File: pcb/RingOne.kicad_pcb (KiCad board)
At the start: 4 copper layers, 0 parts

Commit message: PCB: routing of all components
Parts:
- added BT1: 1S Li-Po, TCY_connectors:Amphenol_10114830-11102LF_1x02_P1.25mm_Horizontal, F.Cu at (126.7, 90.5)
- added C1: 10uF, Capacitor_SMD:C_0805_2012Metric, F.Cu at (127.0, 101.0)
- added C10: 100nF, TCY_passives:C_0603_1608Metric, F.Cu at (129.0, 95.9)
- added C11: 100nF, Capacitor_SMD:C_0603_1608Metric, B.Cu at (131.5, 99.8)
- added C12: 100nF, Capacitor_SMD:C_0603_1608Metric, F.Cu at (114.4, 102.0)
- added C13: 1uF, Capacitor_SMD:C_0603_1608Metric, F.Cu at (110.8, 88.1)
- added C14: 1uF, Capacitor_SMD:C_0603_1608Metric, F.Cu at (121.7, 87.6)
- added C15: 1uF, Capacitor_SMD:C_0603_1608Metric, F.Cu at (116.3, 86.8)
- added C16: 1uF, Capacitor_SMD:C_0603_1608Metric, F.Cu at (119.4, 86.8)
- added C17: 1uF, Capacitor_SMD:C_0603_1608Metric, B.Cu at (110.5, 88.3)
- added C18: 4.7uF, Capacitor_SMD:C_0603_1608Metric, B.Cu at (132.2, 87.6)
- added C19: 4.7uF, Capacitor_SMD:C_0603_1608Metric, B.Cu at (133.8, 87.6)
- added C2: 100nF, Capacitor_SMD:C_0603_1608Metric, F.Cu at (126.7, 97.3)
- added C20: 100nF, Capacitor_SMD:C_0603_1608Metric, B.Cu at (126.6, 93.0)
- added C21: 100nF, Capacitor_SMD:C_0603_1608Metric, B.Cu at (128.4, 102.8)
- added C22: 1uF, Capacitor_SMD:C_0603_1608Metric, B.Cu at (117.9, 95.5)
- added C23: 100nF, Capacitor_SMD:C_0603_1608Metric, F.Cu at (130.2, 102.0)
- added C24: 100nF, Capacitor_SMD:C_0603_1608Metric, B.Cu at (122.2, 96.3)
- added C25: 1uF, Capacitor_SMD:C_0603_1608Metric, B.Cu at (117.9, 101.3)
- added C26: 1uF, Capacitor_SMD:C_0603_1608Metric, B.Cu at (120.4, 101.8)
- added C27: 1uF, Capacitor_SMD:C_0603_1608Metric, B.Cu at (123.2, 101.8)
- added C3: 100nF, Capacitor_SMD:C_0603_1608Metric, F.Cu at (115.2, 95.7)
- added C4: 100nF, Capacitor_SMD:C_0603_1608Metric, F.Cu at (126.7, 102.8)
- added C5: 100nF, Capacitor_SMD:C_0603_1608Metric, F.Cu at (115.2, 98.8)
- added C6: 100nF, Capacitor_SMD:C_0603_1608Metric, F.Cu at (132.5, 101.2)
- added C7: 100nF, Capacitor_SMD:C_0603_1608Metric, B.Cu at (106.9, 103.2)
- added C8: 100nF, Capacitor_SMD:C_0603_1608Metric, F.Cu at (132.2, 87.9)
- added C9: 100nF, TCY_passives:C_0603_1608Metric, F.Cu at (129.0, 93.5)
- added D1: LED_RGBA, Resistor_SMD:R_Array_Convex_2x0606, F.Cu at (135.9, 87.9)
- added D2: EADA25L, Package_TO_SOT_SMD:SOT-23, B.Cu at (109.0, 93.5)
- added D3: RB751S40T5G, Diode_SMD:D_SOD-523, B.Cu at (129.5, 99.0)
- added D4: RB751S40T5G, Diode_SMD:D_SOD-523, B.Cu at (129.5, 100.6)
- added D5: 3V3, Diode_SMD:D_SOD-523, B.Cu at (129.5, 97.4)
- added D6: 3V3, Diode_SMD:D_SOD-523, B.Cu at (123.7, 96.3)
- added FB1: 50R@100Mhz, Inductor_SMD:L_1206_3216Metric, B.Cu at (109.0, 101.2)
- added J1: PROG_CONN, TCY_connectors:Amphenol_10114830-11103LF_1x03_P1.25mm_Horizontal, B.Cu at (126.5, 90.6)
- added J2: DBG_UART, TCY_connectors:Amphenol_10114830-11103LF_1x03_P1.25mm_Horizontal, B.Cu at (116.5, 90.6)
- added J3: USB_C_Receptacle_USB2.0, Connector_USB:USB_C_Receptacle_HRO_TYPE-C-31-M-12, F.Cu at (109.0, 95.0)
- added Q1: YJQ3400, TCY_IC:UDFN-6-2EP_2x2mm_P0.65mm_EP1x0.7mm, B.Cu at (129.7, 94.0)
- added Q2: UT6MA2TCR, TCY_IC:UDFN-6-2EP_2x2mm_P0.65mm_EP1x0.7mm, B.Cu at (126.6, 96.7)
- added R1: 100k, Resistor_SMD:R_0603_1608Metric, B.Cu at (105.9, 100.9)
- added R10: 330R, Resistor_SMD:R_0603_1608Metric, F.Cu at (129.5, 91.4)
- added R11: 2k2, Resistor_SMD:R_0603_1608Metric, B.Cu at (126.6, 94.7)
- added R12: 470k, Resistor_SMD:R_0603_1608Metric, B.Cu at (126.7, 100.7)
- added R13: 470k, Resistor_SMD:R_0603_1608Metric, B.Cu at (126.7, 99.2)
- added R14: 10k, Resistor_SMD:R_0603_1608Metric, F.Cu at (130.6, 97.4)
- added R15: 10k, Resistor_SMD:R_0603_1608Metric, F.Cu at (130.6, 94.5)
- added R16: 100k, Resistor_SMD:R_0603_1608Metric, B.Cu at (117.0, 93.6)
- added R17: 1k, Resistor_SMD:R_0603_1608Metric, F.Cu at (132.5, 102.8)
- added R18: 0.05R, Resistor_SMD:R_0603_1608Metric, B.Cu at (120.7, 98.8)
- added R19: 10k, Resistor_SMD:R_0603_1608Metric, B.Cu at (132.3, 97.4)
- added R2: 1k, Resistor_SMD:R_0603_1608Metric, B.Cu at (109.9, 103.2)
- added R3: 22R, Resistor_SMD:R_0603_1608Metric, B.Cu at (106.0, 94.4)
- added R4: 22R, Resistor_SMD:R_0603_1608Metric, B.Cu at (106.0, 97.4)
- added R5: 1k, Resistor_SMD:R_0603_1608Metric, B.Cu at (108.9, 88.3)
- added R6: 10k, TCY_passives:R_0603_1608Metric, F.Cu at (108.3, 88.7)
- added R7: 1k, TCY_passives:R_0603_1608Metric, F.Cu at (108.3, 87.6)
- added R8: 22k, Resistor_SMD:R_0603_1608Metric, B.Cu at (135.1, 91.5)
- added R9: 100k, Resistor_SMD:R_0603_1608Metric, B.Cu at (133.0, 89.9)
- added SW1: RST_BTN, TCY_buttons_switches:KMT031NGJLHS, F.Cu at (107.2, 102.0)
- added SW2: WAKEUP, TCY_buttons_switches:EVQ-P7J01P, F.Cu at (136.8, 102.4)
- added TP1: VBUS, TCY_connectors:TestPoint_Pad_D0.5mm, F.Cu at (106.5, 89.1)
- added TP2: TestPoint, TCY_connectors:TestPoint_Pad_D0.5mm, B.Cu at (126.3, 101.9)
- added TP3: TestPoint, TCY_connectors:TestPoint_Pad_D0.5mm, B.Cu at (132.8, 96.1)
- added U1: STM32L452CEUx, Package_DFN_QFN:QFN-48-1EP_7x7mm_P0.5mm_EP5.6x5.6mm, F.Cu at (120.4, 99.1)
- added U10: MCP73831-2-OT, Package_TO_SOT_SMD:SOT-23-5, B.Cu at (136.2, 88.2)
- added U11: BQ297xy, Package_SON:WSON-6_1.5x1.5mm_P0.5mm, B.Cu at (129.8, 91.6)
- added U12: LM66100, Package_TO_SOT_SMD:SOT-363_SC-70-6, B.Cu at (113.9, 93.5)
- added U13: LM66100, Package_TO_SOT_SMD:SOT-363_SC-70-6, B.Cu at (113.9, 96.5)
- added U14: SN74LVC1G14DRL, Package_TO_SOT_SMD:SOT-553, B.Cu at (131.1, 102.5)
- added U15: NCV8165ML330, Package_DFN_QFN:DFN-8-1EP_3x3mm_P0.65mm_EP1.55x2.4mm, B.Cu at (118.2, 98.5)
- added U16: INA199, Package_DFN_QFN:UQFN-10_1.4x1.8mm_P0.4mm, B.Cu at (122.8, 99.0)
- added U17: MIC94300, TCY_IC:MLF-4_1.2x1.6mm_P0.5_1EP_0.85x0.5mm, B.Cu at (121.8, 101.7)
- added U2: RN4871, RF_Module:Microchip_RN4871, F.Cu at (136.0, 95.0)
- added U3: M24C32-FMC6TG, Package_DFN_QFN:DFN-8-1EP_3x2mm_P0.5mm_EP1.3x1.5mm, F.Cu at (111.5, 102.0)
- added U4: KTD2026BEWE, TCY_IC:UTDFN-8-1EP_1.5x1.5mm_P0.4mm_EP0.8x1.45mm, F.Cu at (133.9, 88.2)
- added U5: LSM6DSL, Package_LGA:LGA-14_3x2.5mm_P0.5mm_LayoutBorder3x4y, F.Cu at (126.7, 94.5)
- added U6: AT25SF321B, Package_DFN_QFN:DFN-8-1EP_6x5mm_P1.27mm_EP4x4mm, B.Cu at (136.0, 101.0)
- added U7: USBLC6-2SC6, Package_TO_SOT_SMD:SOT-23-6, B.Cu at (109.0, 97.0)
- added U8: PMDPB70XP, TCY_IC:UDFN-6-2EP_2x2mm_P0.65mm_EP1x0.7mm, F.Cu at (113.0, 88.0)
- added U9: STUSB1600AQTR, Package_DFN_QFN:QFN-24-1EP_4x4mm_P0.5mm_EP2.7x2.7mm, F.Cu at (118.3, 90.2)
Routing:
- net GND: track 0.00 -> 171.3 mm, vias 0 -> 70
- net +3V3: track 0.00 -> 118.5 mm, vias 0 -> 10
- net +BATT: track 0.00 -> 53.3 mm, vias 0 -> 5
- net /PER_PWR: track 0.00 -> 52.5 mm, vias 0 -> 4
- net /SDA: track 0.00 -> 44.4 mm, vias 0 -> 3
- net /SCL: track 0.00 -> 43.2 mm, vias 0 -> 3
- net VBUS: track 0.00 -> 40.1 mm, vias 0 -> 3
- net /RESET: track 0.00 -> 36.7 mm, vias 0 -> 3
- net VCC: track 0.00 -> 34.8 mm, vias 0 -> 2
- net /CHARG_STAT: track 0.00 -> 33.6 mm, vias 0 -> 2
- net +5V: track 0.00 -> 33.1 mm, vias 0 -> 5
- net /MOSI: track 0.00 -> 32.5 mm, vias 0 -> 2
- net /SCK: track 0.00 -> 29.6 mm, vias 0 -> 4
- net /Power_management/PWR_EN: track 0.00 -> 29.4 mm, vias 0 -> 2
- net /MISO: track 0.00 -> 23.2 mm, vias 0 -> 2
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- added copper zone on B.Cu, net GND
- added copper zone on F.Cu, net GND
- added copper zone on In1.Cu, net GND
- added copper zone on In2.Cu, net GND
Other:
- board outline added: 35 x 18 mm
- board text added: "JLCJLCJLCJLC"

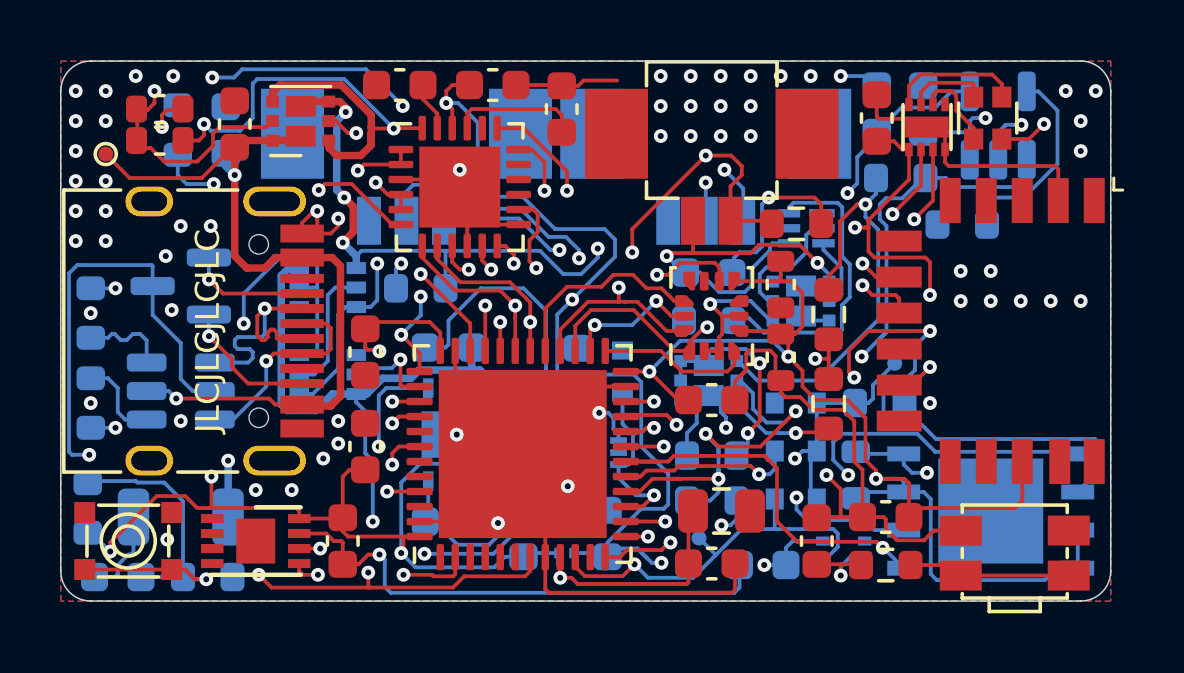
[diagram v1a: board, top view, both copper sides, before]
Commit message: PCB & Schema: update page layout
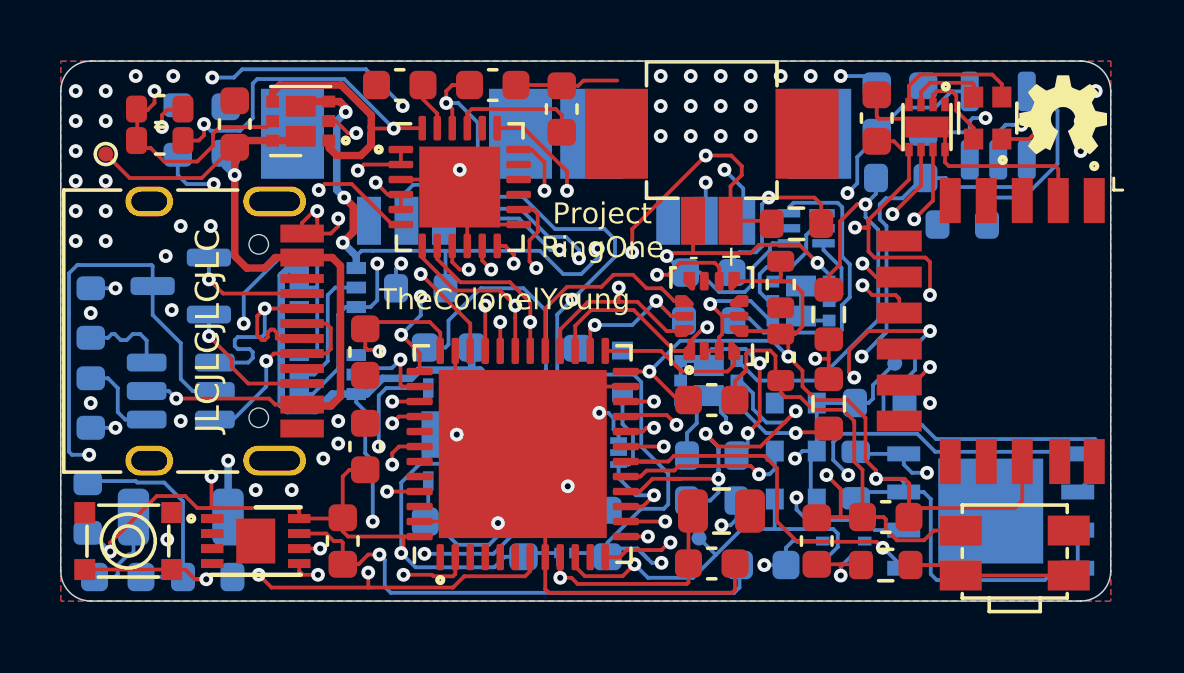
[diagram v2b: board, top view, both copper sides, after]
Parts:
- added G***: LOGO, LOGO, F.Cu at (138.4, 87.8)
- added G***: LOGO, LOGO, B.Cu at (136.8, 95.2)
- added G***: LOGO, LOGO, B.Cu at (115.0, 100.8)
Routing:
- net GND: vias 70 -> 63
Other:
- board text added: "+"
- board text added: "-"
- board text added: "C"
- board text added: "G"
- board text added: "I"
- board text added: "Project RingOne"
- board text added: "R"
- board text added: "T"
- board text added: "TheColonelYoung"
- board text added: "v1.0 01/2021"

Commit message: Schema & PCB: add pull up to wakeup button
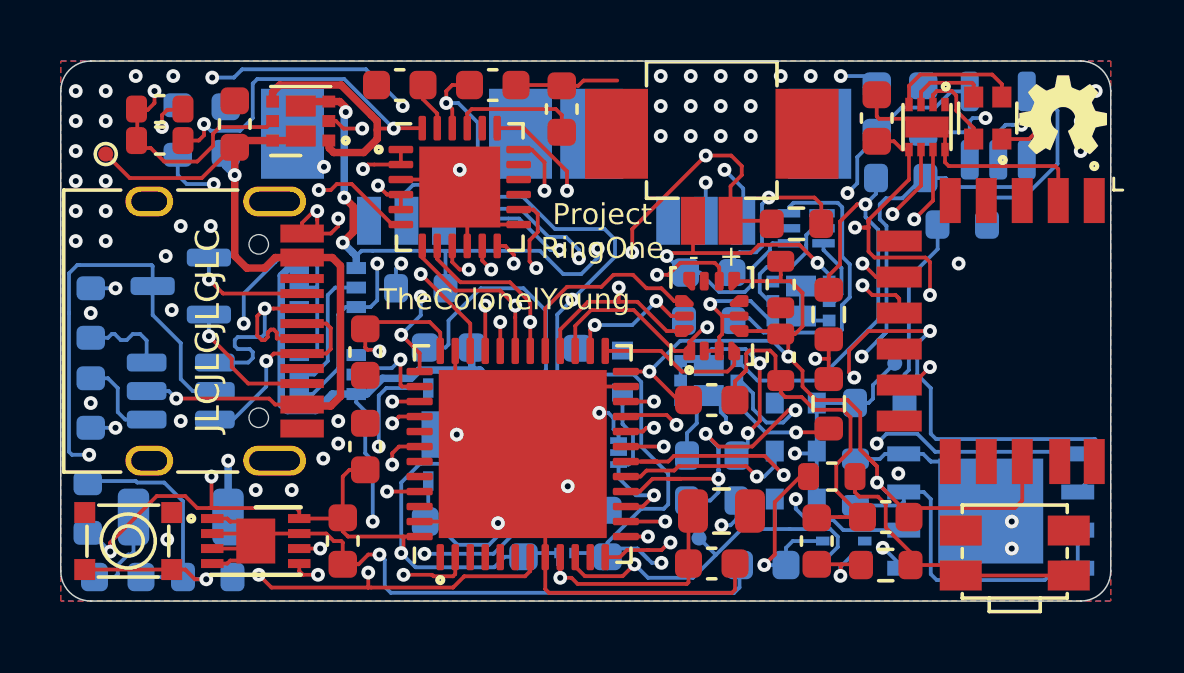
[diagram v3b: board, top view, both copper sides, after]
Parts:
- added R20: 100k, TCY_passives:R_0603_1608Metric, F.Cu at (130.7, 99.8)
- C11: footprint Capacitor_SMD:C_0603_1608Metric -> TCY_passives:C_0603_1608Metric
- moved C11 0.24 mm to (131.5, 100.0)
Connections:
- BT1 pad ~: (no net) -> GND
- J1 pad ~: (no net) -> GND
- J2 pad ~: (no net) -> GND
- U3 pad 9: (no net) -> GND
- U6 pad 9: (no net) -> GND
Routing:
- net GND: track 171.3 -> 183.5 mm, vias 63 -> 65
- net /MOSI: track 32.5 -> 28.4 mm
- net Net-(R17-Pad2): track 5.42 -> 9.50 mm
- net VCC: track 34.8 -> 38.5 mm
- net /SCK: track 29.6 -> 27.7 mm
- net /Power_management/PWR_EN: track 29.4 -> 27.7 mm
- net /CHARG_STAT: track 33.6 -> 32.5 mm
- net /MISO: track 23.2 -> 22.7 mm
- net Net-(R6-Pad1): track 18.8 -> 18.3 mm
- net /CS_FLASH: vias 1 -> 2

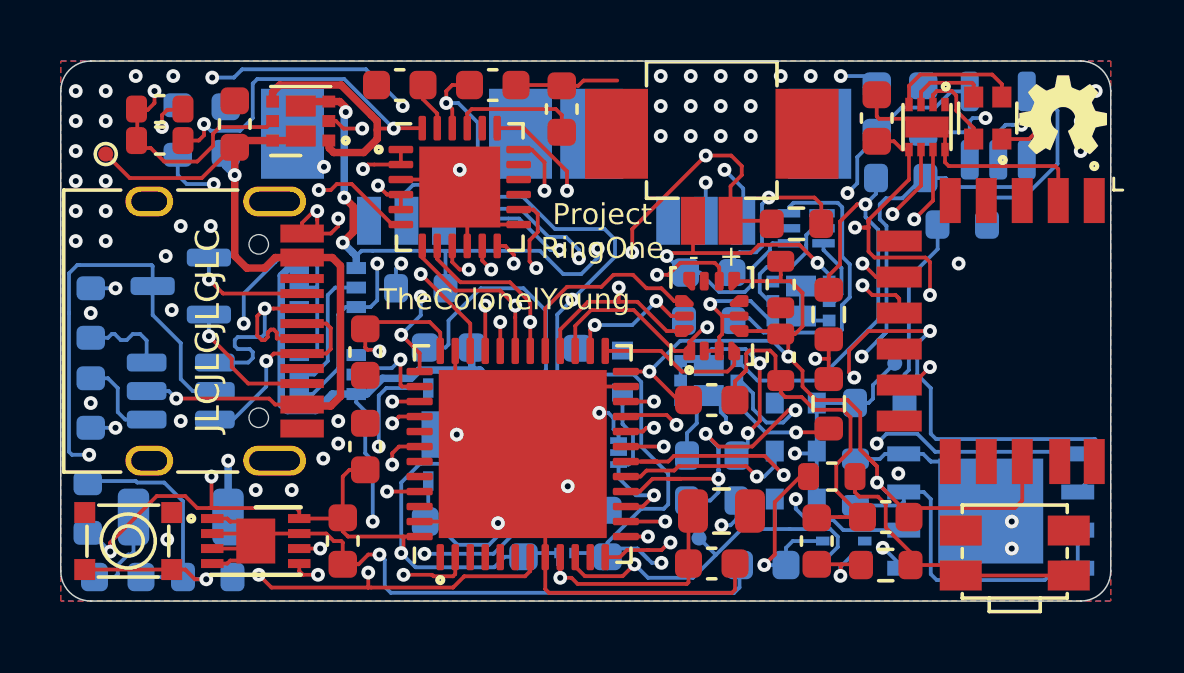
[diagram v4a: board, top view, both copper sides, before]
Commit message: Schema & PCB: Update page layout, add notes about SPI modes and I2C addresses
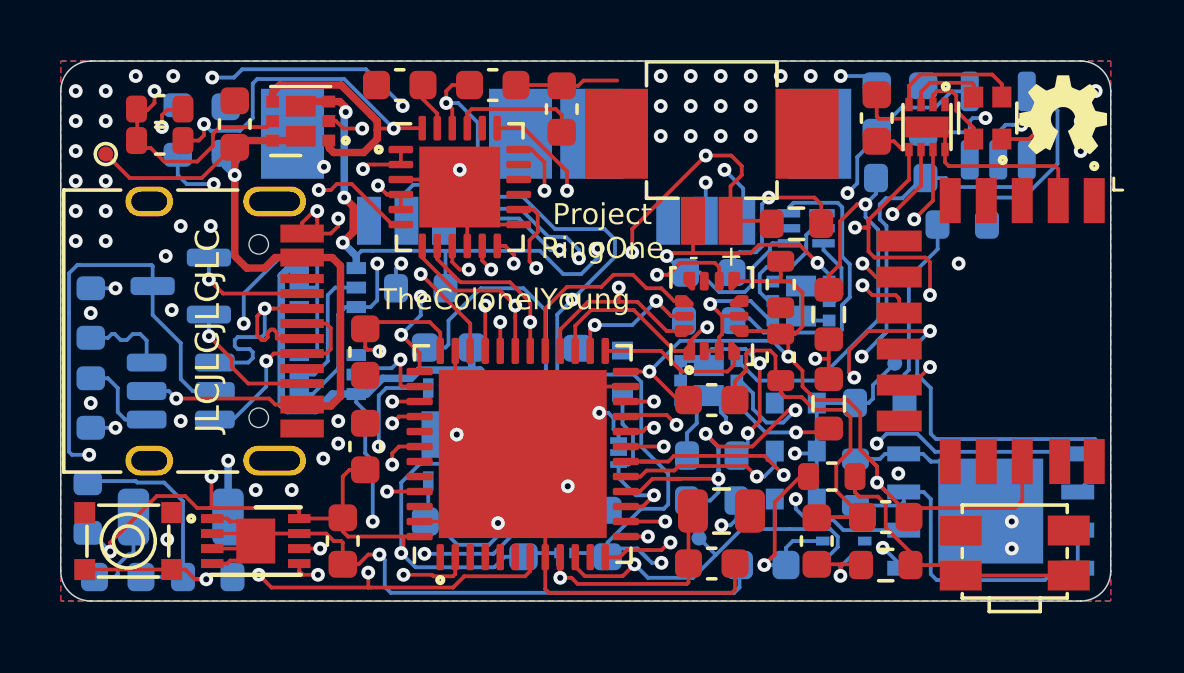
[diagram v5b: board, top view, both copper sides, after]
